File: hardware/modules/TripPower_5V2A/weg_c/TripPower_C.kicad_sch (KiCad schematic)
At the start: 26 parts, among them J1 Vehicle_IN, J2 TripTracer_IO, Q1 AUIRFS6535TRL, Q2 AUIRFS6535TRL, U1 AP74502HQTA8-7, U2 TPS26631PWPR, U3 TPSM33620S5QRDNRQ1

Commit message: bom(trippower-c): select temperature-capable in-stock KEMET MLCC MPNs without claiming DC-bias validation
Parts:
- C3: MPN TBD_50V_X7R -> C1210C105K5RACAUTO
- C4: MPN TBD_50V_X7R -> C1210C475K5RACAUTO
- C5, C9: MPN TBD_50V_X7R -> C1206C104K5RACTU
- C6: MPN TBD_16V_X7R -> C1206C105K4RACTU
- C7, C8: MPN TBD_16V_X7R -> C1210C226K4RACTU
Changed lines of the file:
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@@
 (property "Value" "1u 50V eFuse OUT" (at 225 217.54 0) (effects (font (size 1.02 1.02))))
 (property "Footprint" "Capacitor_SMD:C_1210_3225Metric" (at 225 215 0) (effects (font (size 1 1)) (hide yes)))
-(property "MPN" "TBD_50V_X7R" (at 225 215 0) (effects (font (size 1 1)) (hide yes)))
+(property "MPN" "C1210C105K5RACAUTO" (at 225 215 0) (effects (font (size 1 1)) (hide yes)))
 (instances (project "TripPower_C" (path "/a3cd0426-2026-4000-8000-000000000001" (reference "C3") (unit 1)))))
 (symbol (lib_id "TripPowerC:C") (at 265 215 0) (unit 1) (in_bom yes) (on_board yes) (dnp no)
@@
 (property "Value" "4u7 50V IN" (at 265 217.54 0) (effects (font (size 1.02 1.02))))
 (property "Footprint" "Capacitor_SMD:C_1210_3225Metric" (at 265 215 0) (effects (font (size 1 1)) (hide yes)))
-(property "MPN" "TBD_50V_X7R" (at 265 215 0) (effects (font (size 1 1)) (hide yes)))
+(property "MPN" "C1210C475K5RACAUTO" (at 265 215 0) (effects (font (size 1 1)) (hide yes)))
 (instances (project "TripPower_C" (path "/a3cd0426-2026-4000-8000-000000000001" (reference "C4") (unit 1)))))
 (symbol (lib_id "TripPowerC:C") (at 305 215 0) (unit 1) (in_bom yes) (on_board yes) (dnp no)
@@
 (property "Value" "100n 50V HF" (at 305 217.54 0) (effects (font (size 1.02 1.02))))
 (property "Footprint" "Capacitor_SMD:C_1206_3216Metric" (at 305 215 0) (effects (font (size 1 1)) (hide yes)))
-(property "MPN" "TBD_50V_X7R" (at 305 215 0) (effects (font (size 1 1)) (hide yes)))
+(property "MPN" "C1206C104K5RACTU" (at 305 215 0) (effects (font (size 1 1)) (hide yes)))
 (instances (project "TripPower_C" (path "/a3cd0426-2026-4000-8000-000000000001" (reference "C5") (unit 1)))))
 (symbol (lib_id "TripPowerC:C") (at 345 215 0) (unit 1) (in_bom yes) (on_board yes) (dnp no)
@@
 (property "Value" "1u 16V VCC" (at 345 217.54 0) (effects (font (size 1.02 1.02))))
 (property "Footprint" "Capacitor_SMD:C_1206_3216Metric" (at 345 215 0) (effects (font (size 1 1)) (hide yes)))
-(property "MPN" "TBD_16V_X7R" (at 345 215 0) (effects (font (size 1 1)) (hide yes)))
+(property "MPN" "C1206C105K4RACTU" (at 345 215 0) (effects (font (size 1 1)) (hide yes)))
 (instances (project "TripPower_C" (path "/a3cd0426-2026-4000-8000-000000000001" (reference "C6") (unit 1)))))
 (symbol (lib_id "TripPowerC:C") (at 65 241 0) (unit 1) (in_bom yes) (on_board yes) (dnp no)
@@
 (property "Value" "22u 16V OUT" (at 65 243.54 0) (effects (font (size 1.02 1.02))))
 (property "Footprint" "Capacitor_SMD:C_1210_3225Metric" (at 65 241 0) (effects (font (size 1 1)) (hide yes)))
-(property "MPN" "TBD_16V_X7R" (at 65 241 0) (effects (font (size 1 1)) (hide yes)))
+(property "MPN" "C1210C226K4RACTU" (at 65 241 0) (effects (font (size 1 1)) (hide yes)))
 (instances (project "TripPower_C" (path "/a3cd0426-2026-4000-8000-000000000001" (reference "C7") (unit 1)))))
 (symbol (lib_id "TripPowerC:C") (at 105 241 0) (unit 1) (in_bom yes) (on_board yes) (dnp no)
@@
 (property "Value" "22u 16V OUT" (at 105 243.54 0) (effects (font (size 1.02 1.02))))
 (property "Footprint" "Capacitor_SMD:C_1210_3225Metric" (at 105 241 0) (effects (font (size 1 1)) (hide yes)))
-(property "MPN" "TBD_16V_X7R" (at 105 241 0) (effects (font (size 1 1)) (hide yes)))
+(property "MPN" "C1210C226K4RACTU" (at 105 241 0) (effects (font (size 1 1)) (hide yes)))
 (instances (project "TripPower_C" (path "/a3cd0426-2026-4000-8000-000000000001" (reference "C8") (unit 1)))))
 (symbol (lib_id "TripPowerC:C") (at 145 241 0) (unit 1) (in_bom yes) (on_board yes) (dnp no)
@@
 (property "Value" "100n 50V EF_IN" (at 145 243.54 0) (effects (font (size 1.02 1.02))))
 (property "Footprint" "Capacitor_SMD:C_1206_3216Metric" (at 145 241 0) (effects (font (size 1 1)) (hide yes)))
-(property "MPN" "TBD_50V_X7R" (at 145 241 0) (effects (font (size 1 1)) (hide yes)))
+(property "MPN" "C1206C104K5RACTU" (at 145 241 0) (effects (font (size 1 1)) (hide yes)))
 (instances (project "TripPower_C" (path "/a3cd0426-2026-4000-8000-000000000001" (reference "C9") (unit 1)))))
 (embedded_fonts no)

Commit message: refactor(trippower-c): choose stocked 300V 97mohm Vishay MOSFET and align pulse math to 10.2k
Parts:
- Q1, Q2: value AUIRFS6535TRL -> SQM35N30-97_GE3; MPN AUIRFS6535TRL -> SQM35N30-97_GE3
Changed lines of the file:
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@@
 (symbol (lib_id "TripPowerC:FET_N_D2PAK") (at 65 90 0) (unit 1) (in_bom yes) (on_board yes) (dnp no)
 (property "Reference" "Q1" (at 65 62 0) (effects (font (size 1.27 1.27))))
-(property "Value" "AUIRFS6535TRL" (at 65 92.54 0) (effects (font (size 1.02 1.02))))
+(property "Value" "SQM35N30-97_GE3" (at 65 92.54 0) (effects (font (size 1.02 1.02))))
 (property "Footprint" "Package_TO_SOT_SMD:TO-263-3_TabPin2" (at 65 90 0) (effects (font (size 1 1)) (hide yes)))
-(property "MPN" "AUIRFS6535TRL" (at 65 90 0) (effects (font (size 1 1)) (hide yes)))
+(property "MPN" "SQM35N30-97_GE3" (at 65 90 0) (effects (font (size 1 1)) (hide yes)))
 (instances (project "TripPower_C" (path "/a3cd0426-2026-4000-8000-000000000001" (reference "Q1") (unit 1)))))
 (symbol (lib_id "TripPowerC:FET_N_D2PAK") (at 120 90 0) (unit 1) (in_bom yes) (on_board yes) (dnp no)
 (property "Reference" "Q2" (at 120 62 0) (effects (font (size 1.27 1.27))))
-(property "Value" "AUIRFS6535TRL" (at 120 92.54 0) (effects (font (size 1.02 1.02))))
+(property "Value" "SQM35N30-97_GE3" (at 120 92.54 0) (effects (font (size 1.02 1.02))))
 (property "Footprint" "Package_TO_SOT_SMD:TO-263-3_TabPin2" (at 120 90 0) (effects (font (size 1 1)) (hide yes)))
-(property "MPN" "AUIRFS6535TRL" (at 120 90 0) (effects (font (size 1 1)) (hide yes)))
+(property "MPN" "SQM35N30-97_GE3" (at 120 90 0) (effects (font (size 1 1)) (hide yes)))
 (instances (project "TripPower_C" (path "/a3cd0426-2026-4000-8000-000000000001" (reference "Q2") (unit 1)))))
 (symbol (lib_id "TripPowerC:AP74502HQ") (at 85 140 0) (unit 1) (in_bom yes) (on_board yes) (dnp no)

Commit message: feat(trippower-c): add 4.7uF VIN and 22uF 5V MLCC margin positions due DC bias
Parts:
- added C10: 4u7 50V VIN RESERVE, Capacitor_SMD:C_1210_3225Metric, symbol TripPowerC:C
- added C11: 22u 16V OUT RESERVE, Capacitor_SMD:C_1210_3225Metric, symbol TripPowerC:C
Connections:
- net +5V_TRIPPOWER: now also C11.1 (A)
- net GND: now also C10.2 (B), C11.2 (B)
- net RAW_PROTECTED: now also C10.1 (A)
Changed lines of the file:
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@@
 (property "MPN" "C1206C104K5RACTU" (at 145 241 0) (effects (font (size 1 1)) (hide yes)))
 (instances (project "TripPower_C" (path "/a3cd0426-2026-4000-8000-000000000001" (reference "C9") (unit 1)))))
+(symbol (lib_id "TripPowerC:C") (at 185 241 0) (unit 1) (in_bom yes) (on_board yes) (dnp no)
+(property "Reference" "C10" (at 185 213 0) (effects (font (size 1.27 1.27))))
+(property "Value" "4u7 50V VIN RESERVE" (at 185 243.54 0) (effects (font (size 1.02 1.02))))
+(property "Footprint" "Capacitor_SMD:C_1210_3225Metric" (at 185 241 0) (effects (font (size 1 1)) (hide yes)))
+(property "MPN" "C1210C475K5RACAUTO" (at 185 241 0) (effects (font (size 1 1)) (hide yes)))
+(instances (project "TripPower_C" (path "/a3cd0426-2026-4000-8000-000000000001" (reference "C10") (unit 1)))))
+(wire (pts (xy 174.84 241) (xy 171.03 241)) (stroke (width 0) (type default)))
+(label "RAW_PROTECTED" (at 171.03 241 0) (effects (font (size 1 1)) (justify left bottom)))
+(wire (pts (xy 195.16 241) (xy 198.97 241)) (stroke (width 0) (type default)))
+(label "GND" (at 198.97 241 0) (effects (font (size 1 1)) (justify left bottom)))
+(symbol (lib_id "TripPowerC:C") (at 225 241 0) (unit 1) (in_bom yes) (on_board yes) (dnp no)
+(property "Reference" "C11" (at 225 213 0) (effects (font (size 1.27 1.27))))
+(property "Value" "22u 16V OUT RESERVE" (at 225 243.54 0) (effects (font (size 1.02 1.02))))
+(property "Footprint" "Capacitor_SMD:C_1210_3225Metric" (at 225 241 0) (effects (font (size 1 1)) (hide yes)))
+(property "MPN" "C1210C226K4RACTU" (at 225 241 0) (effects (font (size 1 1)) (hide yes)))
+(instances (project "TripPower_C" (path "/a3cd0426-2026-4000-8000-000000000001" (reference "C11") (unit 1)))))
+(wire (pts (xy 214.84 241) (xy 211.03 241)) (stroke (width 0) (type default)))
+(label "+5V_TRIPPOWER" (at 211.03 241 0) (effects (font (size 1 1)) (justify left bottom)))
+(wire (pts (xy 235.16 241) (xy 238.97 241)) (stroke (width 0) (type default)))
+(label "GND" (at 238.97 241 0) (effects (font (size 1 1)) (justify left bottom)))
 (embedded_fonts no)
 )

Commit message: fix(trippower-c): remove catastrophic 30V connection to TPS26631 SHDN pin13; default open per TI
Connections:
- net HV_PROTECTED: no longer U2.13 (SHDN)
- no-connect marks 11 -> 12
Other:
- note added: "C1-DRAFT / NOT FOR FABRICATION. NATIVE ERC, NETLIST, PIN MAPPING, LAYOUT DRC NOT EXECUTED."
- note added: "REVIEW REQUIRED: U2 SHDN pin13 now FLOAT (internal 2.48..3.3V bias), 200V dynamic still NOT PROVEN; no build."
- note removed: "REVIEW REQUIRED: AP EN backfeed when BAT=0, real HV MOSFET SOA, resistor pulse, IC limits, thermal, eFuse, PCB."
- note removed: "This schematic is a first draft; NATIVE ERC / LAYOUT DRC HAVE NOT BEEN RUN."
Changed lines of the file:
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@@
 (text "TVS / VCAP / INPUT FILTERS" (at 65 204 0) (effects (font (size 1.80 1.80)) (justify left bottom)))
 (text "5V OUT CAPACITORS (50V/16V EFFECTIVE C NOT VERIFIED)" (at 65 231 0) (effects (font (size 1.80 1.80)) (justify left bottom)))
-(text "REVIEW REQUIRED: AP EN backfeed when BAT=0, real HV MOSFET SOA, resistor pulse, IC limits, thermal, eFuse, PCB." (at 21 265 0) (effects (font (size 1.80 1.80)) (justify left bottom)))
-(text "This schematic is a first draft; NATIVE ERC / LAYOUT DRC HAVE NOT BEEN RUN." (at 21 271 0) (effects (font (size 1.80 1.80)) (justify left bottom)))
+(text "REVIEW REQUIRED: U2 SHDN pin13 now FLOAT (internal 2.48..3.3V bias), 200V dynamic still NOT PROVEN; no build." (at 21 265 0) (effects (font (size 1.80 1.80)) (justify left bottom)))
+(text "C1-DRAFT / NOT FOR FABRICATION. NATIVE ERC, NETLIST, PIN MAPPING, LAYOUT DRC NOT EXECUTED." (at 21 271 0) (effects (font (size 1.80 1.80)) (justify left bottom)))
 (wire (pts (xy 53.40 36.92) (xy 57.21 36.92)) (stroke (width 0) (type default)))
 (label "BAT_FUSED_IN" (at 57.21 36.92 0) (effects (font (size 1 1)) (justify left bottom)))
@@
 (no_connect (at 260.40 104.54))
 (no_connect (at 260.40 109.62))
-(wire (pts (xy 260.40 114.70) (xy 264.21 114.70)) (stroke (width 0) (type default)))
-(label "HV_PROTECTED" (at 264.21 114.70 0) (effects (font (size 1 1)) (justify left bottom)))
+(no_connect (at 260.40 114.70))
 (wire (pts (xy 260.40 119.78) (xy 264.21 119.78)) (stroke (width 0) (type default)))
 (label "GND" (at 264.21 119.78 0) (effects (font (size 1 1)) (justify left bottom)))

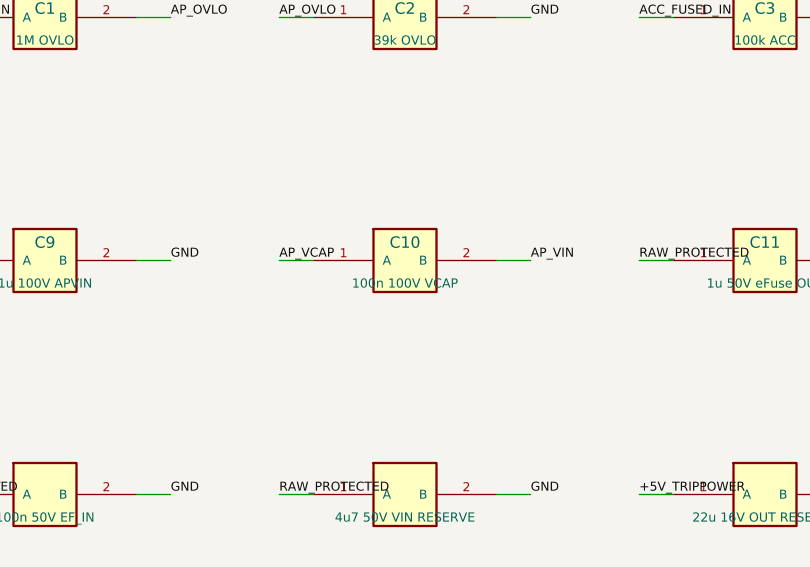
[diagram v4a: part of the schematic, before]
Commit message: fix(trippower-c): align AP VCAP nominal 220nF capacitor to Diodes 200V manufacturer reference
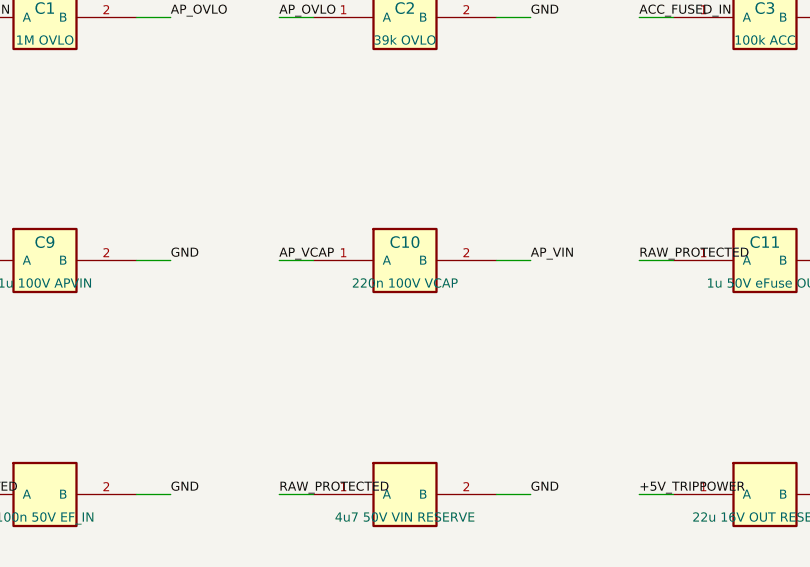
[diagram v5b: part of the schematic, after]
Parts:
- C2: value 100n 100V VCAP -> 220n 100V VCAP; MPN C1206C104K1RACAUTO -> C1206C224K1RACAUTO
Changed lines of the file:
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@@
 (symbol (lib_id "TripPowerC:C") (at 185 215 0) (unit 1) (in_bom yes) (on_board yes) (dnp no)
 (property "Reference" "C2" (at 185 187 0) (effects (font (size 1.27 1.27))))
-(property "Value" "100n 100V VCAP" (at 185 217.54 0) (effects (font (size 1.02 1.02))))
+(property "Value" "220n 100V VCAP" (at 185 217.54 0) (effects (font (size 1.02 1.02))))
 (property "Footprint" "Capacitor_SMD:C_1206_3216Metric" (at 185 215 0) (effects (font (size 1 1)) (hide yes)))
-(property "MPN" "C1206C104K1RACAUTO" (at 185 215 0) (effects (font (size 1 1)) (hide yes)))
+(property "MPN" "C1206C224K1RACAUTO" (at 185 215 0) (effects (font (size 1 1)) (hide yes)))
 (instances (project "TripPower_C" (path "/a3cd0426-2026-4000-8000-000000000001" (reference "C2") (unit 1)))))
 (symbol (lib_id "TripPowerC:C") (at 225 215 0) (unit 1) (in_bom yes) (on_board yes) (dnp no)
